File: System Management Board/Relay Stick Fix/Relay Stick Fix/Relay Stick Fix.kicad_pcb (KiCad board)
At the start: 4 copper layers, 26.8 x 30.2 mm, 13 parts, among them J1 Conn_02x04, J1 Conn_02x04_Odd_Even, J2 Castellations, J2 Structural Header, J3 Structural connector, Q1 NMOS, SW1 SW_SPDT, U1 UCC27511ADBV

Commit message: before layout revision
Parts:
- removed the J1 at (217.9, 89.2)
- removed J2: Castellations, PSA:EE2-5NU Castellated
- removed J2: Structural Header, Connector_PinHeader_2.54mm:PinHeader_2x04_P2.54mm_Vertical_SMD
- removed J3: Structural connector, Connector_PinSocket_2.54mm:PinSocket_2x04_P2.54mm_Vertical_SMD
- removed JP1: Jumper_2_Open, Jumper:SolderJumper-2_P1.3mm_Open_Pad1.0x1.5mm
- removed SW1: SW_SPDT, Package_TO_SOT_SMD:SOT-23
- removed TP1: TestPoint, TestPoint:TestPoint_Pad_D2.0mm
- added C2: 10uF, Capacitor_SMD:C_1206_3216Metric_Pad1.33x1.80mm_HandSolder, F.Cu at (214.0, 141.4)
- added H1: MountingHole_Pad, MountingHole:MountingHole_3.2mm_M3_DIN965_Pad, F.Cu at (221.5, 132.2)
- added R3: 0, Resistor_SMD:R_1206_3216Metric_Pad1.30x1.75mm_HandSolder, F.Cu at (218.7, 142.6)
- C1: value C -> 100nF
- J1: footprint Connector_PinHeader_2.54mm:PinHeader_2x04_P2.54mm_Vertical_SMD -> Connector_PinHeader_2.54mm:PinHeader_2x06_P2.54mm_Vertical_SMD
- R1: value R -> 5.1k
- R2: value R -> 0
- U1: value UCC27511ADBV -> ~; footprint Package_TO_SOT_SMD:SOT-143 -> Package_DIP:DIP-8_W8.89mm_SMDSocket_LongPads
- moved Q1 54.3 mm to (223.7, 122.5), turned to 0 degrees
- moved J1 49.8 mm to (206.5, 126.8)
- moved C1 45.3 mm to (210.6, 141.4)
- moved R1 42.7 mm to (206.1, 139.2), turned to 0 degrees
- moved R2 42.2 mm to (215.8, 136.2), turned to 0 degrees
- moved U1 40.5 mm to (209.2, 125.3), turned to 90 degrees
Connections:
- C1 pad 1: Net-(Q1-G) -> Net-(U1-TIMER)
- J1 pad 5: /i3 -> unconnected-(J1-Pin_5-Pad5)
- J1 pad 6: /i3 -> unconnected-(J1-Pin_6-Pad6)
- J1 pad 7: /Vbat Prot -> /i3
- J1 pad 8: /Vbat Prot -> /i3
- Q1 pad 5: /Vbat Prot -> Net-(Q1-D)
- R1 pad 2: Net-(SW1-C) -> /Fault
- R2 pad 1: Net-(SW1-A) -> Net-(U1-GATE)
- R2 pad 2: GND -> Net-(Q1-G)
- U1 pad 1: unconnected-(U1-V_{DD}-Pad1) -> GND
- U1 pad 2: unconnected-(U1-OUTH-Pad2) -> Net-(U1-TIMER)
- U1 pad 3: unconnected-(U1-OUTL-Pad3) -> /Fault
- U1 pad 4: unconnected-(U1-GND-Pad4) -> /5V Bootstrap
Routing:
- net Net-(Q1-D): track 0.00 -> 41.0 mm
- net /Vbat Prot: track 11.3 -> 37.8 mm, vias 1 -> 2
- net Net-(U1-GATE): track 0.00 -> 22.5 mm
- net /Fault: track 0.00 -> 16.7 mm
- net Net-(Q1-G): track 29.0 -> 13.3 mm
- net /5V Bootstrap: track 19.8 -> 33.6 mm
- net Net-(U1-TIMER): track 0.00 -> 11.2 mm
- net Net-(SW1-A): track 10.0 -> 0.00 mm
- net Net-(SW1-C): track 5.44 -> 0.00 mm
- net /i3: track 20.1 -> 21.5 mm
- net GND: track 1.89 -> 2.66 mm, vias 6 -> 2
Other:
- board size 26.8 x 30.2 mm -> 28.2 x 29 mm
- board text added: "SM-V0.3 RL Fx Q1 2025"
- board text removed: "Outline of the Castellated Layer Below"
- board text removed: "SM-V0.3 NMOS RLY Q1 2025"

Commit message: power track redesign
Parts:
- R3: footprint Resistor_SMD:R_1206_3216Metric_Pad1.30x1.75mm_HandSolder -> Resistor_SMD:R_2512_6332Metric
- U1: footprint Package_DIP:DIP-8_W8.89mm_SMDSocket_LongPads -> Package_SO:SOIC-8-1EP_3.9x4.9mm_P1.27mm_EP2.29x3mm
- moved R3 15.1 mm to (215.6, 127.8), turned to 90 degrees
- moved U1 14.0 mm to (208.4, 139.2), turned to 180 degrees
- moved R2 9.14 mm to (224.4, 139.2), turned to 90 degrees
- moved R1 8.68 mm to (214.8, 139.2), turned to -90 degrees
- moved C1 7.33 mm to (217.6, 139.2), turned to 90 degrees
- moved C2 6.76 mm to (220.4, 139.2)
- moved Q1 1.60 mm to (222.1, 122.7), turned to 180 degrees
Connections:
- net Net-(Q1-D) renamed /Sense
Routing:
- net /Sense: track 41.0 -> 0.00 mm
- net /i3: track 21.5 -> 0.00 mm, vias 1 -> 6
- net /Vbat Prot: track 37.8 -> 22.1 mm, vias 2 -> 6
- net /Fault: track 16.7 -> 4.78 mm
- net Net-(Q1-G): track 13.3 -> 17.7 mm
- net /5V Bootstrap: track 33.6 -> 30.2 mm
- net Net-(U1-TIMER): track 11.2 -> 7.94 mm
- net Net-(U1-GATE): track 22.5 -> 20.1 mm
- net GND: track 2.66 -> 1.70 mm, vias 2 -> 9
- added copper zone on F.Cu, net /Sense
- added copper zone on B.Cu, net /Vbat Prot
- added copper zone on F.Cu, net /Vbat Prot
- added copper zone on B.Cu, net /i3
- added copper zone on F.Cu, net /i3
- added copper zone on B.Cu, net GND
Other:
- board text added: "SMB-V0.3 Relay Replacer Q1 2025"
- board text removed: "SM-V0.3 RL Fx Q1 2025"

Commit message: pwr routed, test points etc
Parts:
- added D1: LED GRN, LED_SMD:LED_1206_3216Metric_Pad1.42x1.75mm_HandSolder, F.Cu at (204.5, 139.3)
- added D2: LED RED, LED_SMD:LED_1206_3216Metric_Pad1.42x1.75mm_HandSolder, F.Cu at (207.5, 139.3)
- added R4: 220, Resistor_SMD:R_1206_3216Metric_Pad1.30x1.75mm_HandSolder, F.Cu at (204.5, 134.1)
- added R5: 220, Resistor_SMD:R_1206_3216Metric_Pad1.30x1.75mm_HandSolder, F.Cu at (207.5, 134.1)
- added TP1: TestPoint, TestPoint:TestPoint_Pad_D1.0mm, F.Cu at (225.9, 134.9)
- added TP2: TestPoint, TestPoint:TestPoint_Pad_D1.0mm, F.Cu at (225.9, 130.6)
- added TP3: TestPoint, TestPoint:TestPoint_THTPad_D1.0mm_Drill0.5mm, F.Cu at (212.6, 131.7)
- added TP4: TestPoint, TestPoint:TestPoint_THTPad_D1.0mm_Drill0.5mm, F.Cu at (212.6, 127.4)
- moved U1 5.12 mm to (213.5, 138.8)
- moved C1 4.20 mm to (221.8, 138.6)
- moved C2 4.20 mm to (224.6, 138.6)
- moved R1 4.20 mm to (218.9, 138.6)
- moved R2 3.16 mm to (227.5, 138.6)
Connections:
- net Net-(Q1-G) renamed /Gate
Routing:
- net /Fault: track 4.78 -> 26.7 mm
- net /Sense: track 0.00 -> 21.1 mm, vias 0 -> 27
- net /5V Bootstrap: track 30.2 -> 37.6 mm, vias 1 -> 2
- net /Vbat Prot: track 22.1 -> 18.7 mm, vias 6 -> 7
- net Net-(U1-GATE): track 20.1 -> 23.5 mm, vias 0 -> 2
- net Net-(D2-K): track 0.00 -> 2.21 mm
- net Net-(D1-K): track 0.00 -> 2.21 mm
- net /Gate: track 17.7 -> 19.8 mm
- net Net-(U1-TIMER): track 7.94 -> 7.42 mm
- net GND: track 1.70 -> 1.74 mm, vias 9 -> 7
- net /i3: vias 6 -> 5
- added copper zone on In2.Cu, net /Sense
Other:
- board size 28.2 x 29 mm -> 28.2 x 27 mm
- board text added: "Driver Out"
- board text added: "Fault"
- board text added: "Gate"
- board text added: "ON"
- board text added: "SMB-V0.3 Relay Imprv. Q1 2025"
- board text added: "Vbat_Prot"
- board text added: "Vi3"
- board text added: "d"
- board text added: "g"
- board text added: "s"
- board text removed: "SMB-V0.3 Relay Replacer Q1 2025"

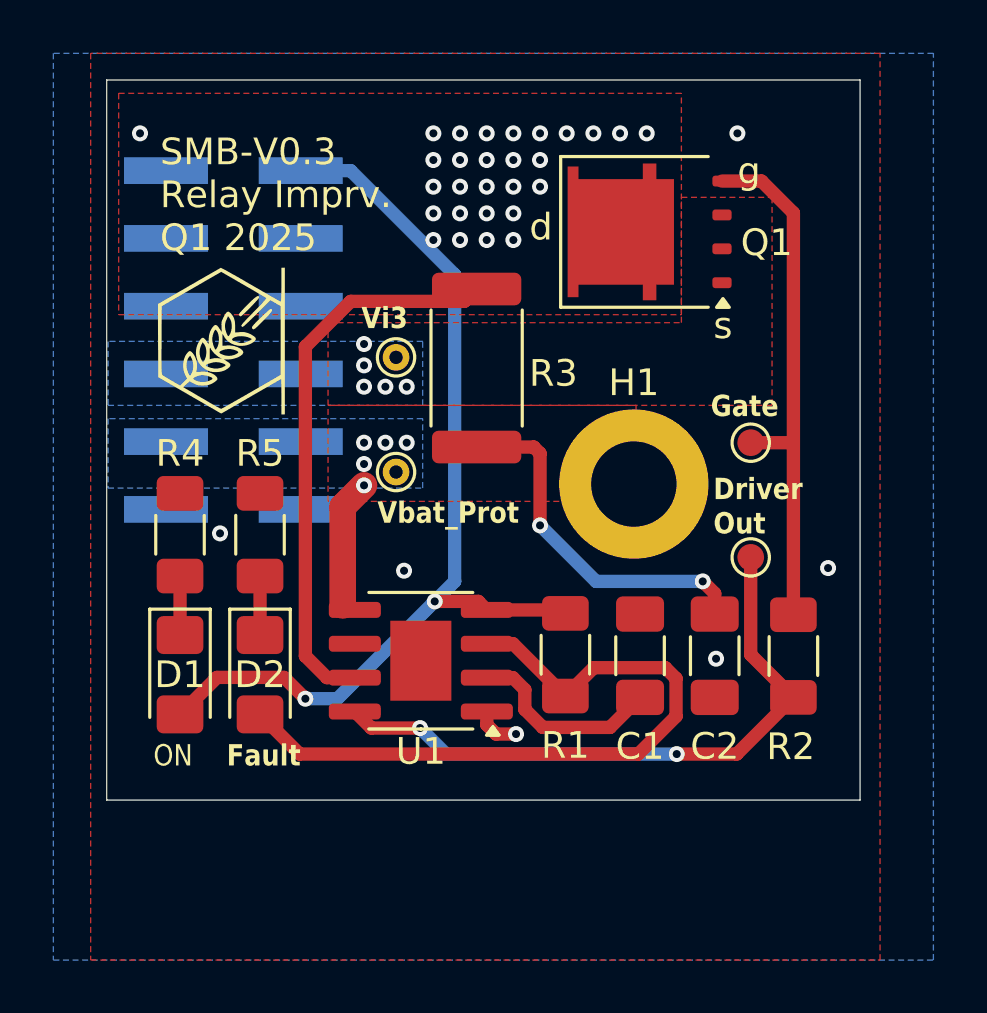
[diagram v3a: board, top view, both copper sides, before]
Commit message: schematic redability improved
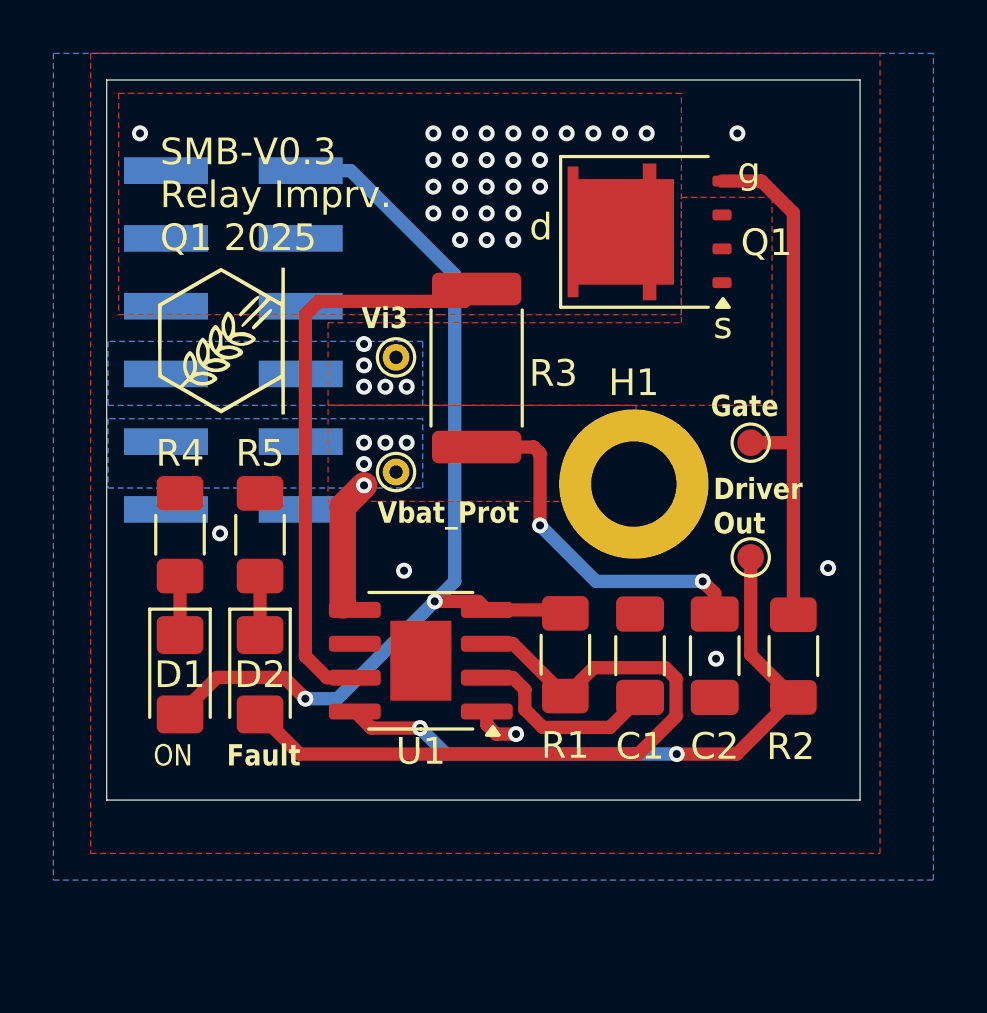
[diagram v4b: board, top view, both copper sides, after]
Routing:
- net /Sense: track 21.1 -> 21.8 mm, vias 27 -> 26
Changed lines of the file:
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@@
 		)
 		(property "Value" "220"
-			(at 0 1.82 270)
+			(at 0 1.82 -90)
 			(layer "F.Fab")
 			(effects
@@
 		)
 		(fp_text user "${REFERENCE}"
-			(at 0 0 270)
+			(at 0 0 -90)
 			(layer "F.Fab")
 			(effects
@@
 		)
 		(property "Value" "220"
-			(at 0 1.82 270)
+			(at 0 1.82 -90)
 			(layer "F.Fab")
 			(effects
@@
 		)
 		(fp_text user "${REFERENCE}"
-			(at 0 0 270)
+			(at 0 0 -90)
 			(layer "F.Fab")
 			(effects
@@
 		)
 		(property "Value" "0"
-			(at 0 1.82 270)
+			(at 0 1.82 -90)
 			(layer "F.Fab")
 			(effects
@@
 		)
 		(fp_text user "${REFERENCE}"
-			(at 0 0 270)
+			(at 0 0 -90)
 			(layer "F.Fab")
 			(effects
@@
 	)
 	(segment
-		(start 215.16 125.3)
-		(end 215.6225 124.8375)
+		(start 211.055 139.41)
+		(end 210.01 139.41)
 		(width 0.5)
 		(layer "F.Cu")
@@
 	)
 	(segment
-		(start 210.01 139.41)
-		(end 209.2 138.6)
+		(start 209.2 138.6)
+		(end 209.2 125.8)
 		(width 0.5)
 		(layer "F.Cu")
@@
 	)
 	(segment
-		(start 209.2 138.6)
-		(end 209.2 127)
+		(start 210.01 139.41)
+		(end 209.2 138.6)
 		(width 0.5)
 		(layer "F.Cu")
@@
 	)
 	(segment
-		(start 210.9 125.3)
-		(end 215.16 125.3)
+		(start 209.2 125.8)
+		(end 209.7 125.3)
 		(width 0.5)
 		(layer "F.Cu")
@@
 	)
 	(segment
-		(start 211.055 139.41)
-		(end 210.01 139.41)
+		(start 209.7 125.3)
+		(end 215.16 125.3)
 		(width 0.5)
 		(layer "F.Cu")
@@
 	)
 	(segment
-		(start 209.2 127)
-		(end 210.9 125.3)
+		(start 215.16 125.3)
+		(end 215.6225 124.8375)
 		(width 0.5)
 		(layer "F.Cu")
@@
 	)
 	(via
-		(at 214 123)
-		(size 0.6)
-		(drill 0.3)
-		(layers "F.Cu" "B.Cu")
-		(free yes)
-		(net 6)
-	)
-	(via
 		(at 216 123)
 		(size 0.6)
@@
 		(polygon
 			(pts
-				(xy 201.15 116) (xy 201.15 150) (xy 230.75 150) (xy 230.75 116)
+				(xy 201.15 116) (xy 201.15 146) (xy 230.75 146) (xy 230.75 116)
 			)
 		)
@@
 		(polygon
 			(pts
-				(xy 199.75 116) (xy 199.75 150) (xy 232.75 150) (xy 232.75 116)
+				(xy 199.75 116) (xy 199.75 147) (xy 232.75 147) (xy 232.75 116)
 			)
 		)
